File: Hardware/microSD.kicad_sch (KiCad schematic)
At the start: 6 parts, among them J3 Micro_SD_Card_Det, Q1 PMOS

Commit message: update
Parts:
- Q1: MPN (none) -> PNM723T201E0
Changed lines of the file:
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@@
+			)
+		)
+		(property "MPN" " PNM723T201E0"
+			(at 84.836 75.438 0)
+			(effects
+				(font
+					(size 1.27 1.27)
+				)
+				(hide yes)
 			)
 		)

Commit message: changes post 3rd review
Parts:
- Q1: footprint Package_TO_SOT_SMD:SOT-723 -> Package_TO_SOT_SMD:SOT-23; MPN PNM723T201E0 -> DMP3099L
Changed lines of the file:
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@@
 			)
 		)
-		(property "Footprint" "Package_TO_SOT_SMD:SOT-723"
+		(property "Footprint" "Package_TO_SOT_SMD:SOT-23"
 			(at 79.756 77.978 0)
 			(effects
@@
 			)
 		)
-		(property "MPN" " PNM723T201E0"
+		(property "MPN" " DMP3099L"
 			(at 84.836 75.438 0)
 			(effects

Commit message: post Andrei review, new SD
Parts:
- removed J3: Micro_SD_Card_Det, Connector_Card:microSD_HC_Hirose_DM3AT-SF-PEJM5, symbol Connector:Micro_SD_Card_Det
- added J9: ST1W008S4TR2000, iclr:JAE_ST1W008S4TR2000, symbol iclr:ST1W008S4TR2000
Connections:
- net SD1_DET is gone; now on net +3V3: R32.2
- net +3V3: no longer R32.1
- net GND: now also J9.GND1 (GND), J9.GND2 (GND), J9.GND3 (GND), J9.GND4 (GND)
- net SD1_CS: now also J9.C2
- net VSPI_MISO: now also J9.C7
- net VSPI_MOSI: now also J9.C3
- net VSPI_SCLK: now also J9.C5
- net at C49.1, JP2.2 (B), Q1.1 (D): now also J9.C4
- new net SD_DET: J9.C6, R32.1
- no-connect marks 2 -> 3
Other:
- moved on the sheet: C49, JP2, Q1, R33

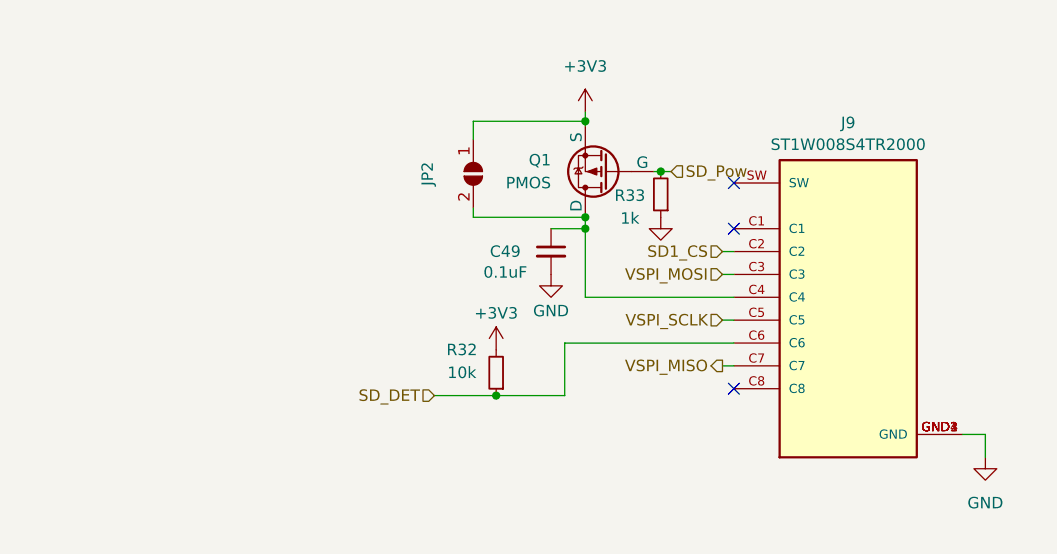
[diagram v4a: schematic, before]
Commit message: changed sd det pinout
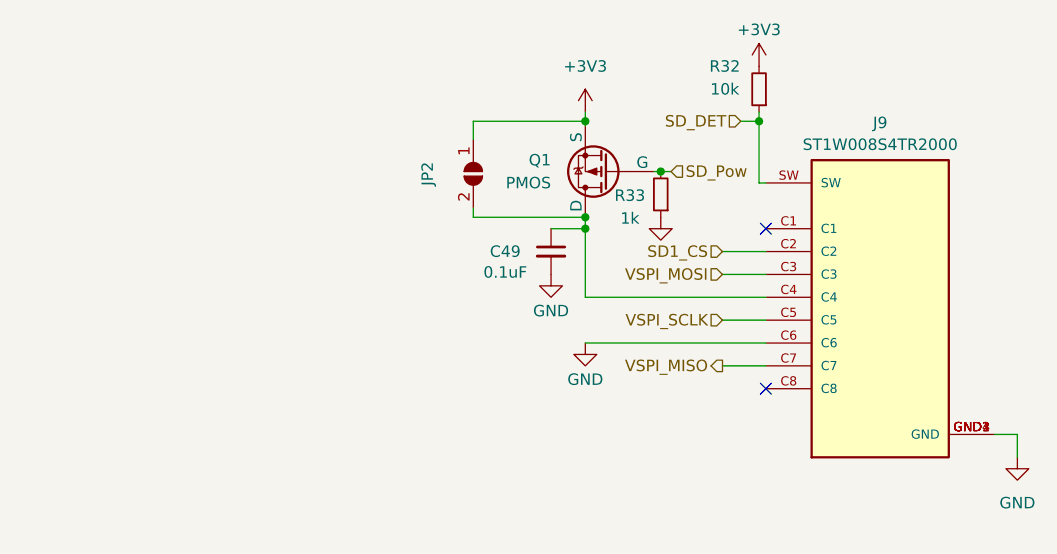
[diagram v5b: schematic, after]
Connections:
- net GND: now also J9.C6
- net SD_DET: now also J9.SW; no longer J9.C6
- no-connect marks 3 -> 2
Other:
- moved on the sheet: J9, R32

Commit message: updated jumpers and silkscreen labelling
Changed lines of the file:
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@@
 (kicad_sch
-	(version 20231120)
+	(version 20250114)
 	(generator "eeschema")
-	(generator_version "8.0")
+	(generator_version "9.0")
 	(paper "A4")
 	(junction
@@
 		(shape input)
 		(at 141.732 94.742 180)
-		(fields_autoplaced yes)
 		(effects
 			(font
@@
 		(shape output)
 		(at 141.732 99.822 180)
-		(fields_autoplaced yes)
 		(effects
 			(font
@@
 		(shape input)
 		(at 141.732 89.662 180)
-		(fields_autoplaced yes)
 		(effects
 			(font
@@
 		(shape input)
 		(at 141.732 87.122 180)
-		(fields_autoplaced yes)
 		(effects
 			(font
@@
 		(shape input)
 		(at 143.764 72.644 180)
-		(fields_autoplaced yes)
 		(effects
 			(font
@@
 		(shape input)
 		(at 136.017 78.232 0)
-		(fields_autoplaced yes)
-		(effects
-			(font
+		(effects
+			(font

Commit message: tidy up schematic and bom
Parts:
- C601: renamed from C49; value 0.1uF -> 100nF
- JP601: renamed from JP2; now left out of the parts list
- Q601: renamed from Q1; value PMOS -> DMP3099L
- R601: renamed from R33; value 1k -> 1kΩ
- R602: renamed from R32; value 10k -> 10kΩ
- renumbered J9 to J601
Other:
- moved on the sheet: JP601
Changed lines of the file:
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@@
 	(wire
 		(pts
-			(xy 114.046 74.676) (xy 114.046 72.644)
+			(xy 110.49 74.93) (xy 110.49 72.644)
 		)
 		(stroke
@@
 	(wire
 		(pts
-			(xy 114.046 83.312) (xy 114.046 82.296)
+			(xy 110.49 83.312) (xy 110.49 82.55)
 		)
 		(stroke
@@
 	(wire
 		(pts
-			(xy 114.046 72.644) (xy 126.492 72.644)
+			(xy 110.49 72.644) (xy 126.492 72.644)
 		)
 		(stroke
@@
 	(wire
 		(pts
-			(xy 126.492 83.312) (xy 114.046 83.312)
+			(xy 126.492 83.312) (xy 110.49 83.312)
 		)
 		(stroke
@@
 		(dnp no)
 		(fields_autoplaced yes)
-		(property "Reference" "#PWR082"
+		(property "Reference" "#PWR0602"
 			(at 126.492 75.438 0)
 			(effects
@@
 			(project "Ricardo-Kermit-Mini"
 				(path "/7db990e4-92e1-4f99-b4d2-435bbec1ba83/d2fb5c72-e348-4618-9c43-b5fd18c57de4"
-					(reference "#PWR082")
+					(reference "#PWR0602")
 					(unit 1)
 				)
@@
 		(on_board yes)
 		(dnp no)
-		(property "Reference" "R32"
+		(property "Reference" "R602"
 			(at 141.986 66.548 0)
 			(effects
@@
 			)
 		)
-		(property "Value" "10k"
+		(property "Value" "10kΩ"
 			(at 141.986 69.088 0)
 			(effects
@@
 			(project "Ricardo-Kermit-Mini"
 				(path "/7db990e4-92e1-4f99-b4d2-435bbec1ba83/d2fb5c72-e348-4618-9c43-b5fd18c57de4"
-					(reference "R32")
+					(reference "R602")
 					(unit 1)
 				)
@@
 	(symbol
 		(lib_id "Jumper:SolderJumper_2_Open")
-		(at 114.046 78.486 270)
+		(at 110.49 78.74 270)
 		(unit 1)
 		(exclude_from_sim no)
-		(in_bom yes)
+		(in_bom no)
 		(on_board yes)
 		(dnp no)
-		(property "Reference" "JP2"
-			(at 108.966 78.486 0)
+		(property "Reference" "JP601"
+			(at 105.41 78.74 0)
 			(effects
 				(font
@@
 		)
 		(property "Value" "SolderJumper_2_Open"
-			(at 82.296 60.706 0)
+			(at 78.74 60.96 0)
 			(effects
 				(font
@@
 		)
 		(property "Footprint" "iclr:SmallerSolderJP"
-			(at 114.046 78.486 0)
+			(at 110.49 78.74 0)
 			(effects
 				(font
@@
 		)
 		(property "Datasheet" "~"
-			(at 114.046 78.486 0)
+			(at 110.49 78.74 0)
 			(effects
 				(font
@@
 		)
 		(property "Description" ""
-			(at 114.046 78.486 0)
+			(at 110.49 78.74 0)
 			(effects
 				(font
@@
 			(project "Ricardo-Kermit-Mini"
 				(path "/7db990e4-92e1-4f99-b4d2-435bbec1ba83/d2fb5c72-e348-4618-9c43-b5fd18c57de4"
-					(reference "JP2")
+					(reference "JP601")
 					(unit 1)
 				)
@@
 		(dnp no)
 		(fields_autoplaced yes)
-		(property "Reference" "#PWR087"
+		(property "Reference" "#PWR0606"
 			(at 174.498 116.332 0)
 			(effects
@@
 			(project "Ricardo-Kermit-Mini"
 				(path "/7db990e4-92e1-4f99-b4d2-435bbec1ba83/d2fb5c72-e348-4618-9c43-b5fd18c57de4"
-					(reference "#PWR087")
+					(reference "#PWR0606")
 					(unit 1)
 				)
@@
 		(on_board yes)
 		(dnp no)
-		(property "Reference" "R33"
+		(property "Reference" "R601"
 			(at 131.445 80.9021 0)
 			(effects
@@
 			)
 		)
-		(property "Value" "1k"
+		(property "Value" "1kΩ"
 			(at 131.445 83.439 0)
 			(effects
@@
 			(project "Ricardo-Kermit-Mini"
 				(path "/7db990e4-92e1-4f99-b4d2-435bbec1ba83/d2fb5c72-e348-4618-9c43-b5fd18c57de4"
-					(reference "R33")
+					(reference "R601")
 					(unit 1)
 				)
@@
 		(dnp no)
 		(fields_autoplaced yes)
-		(property "Reference" "#PWR085"
+		(property "Reference" "#PWR0604"
 			(at 134.874 89.662 0)
 			(effects
@@
 			(project "Ricardo-Kermit-Mini"
 				(path "/7db990e4-92e1-4f99-b4d2-435bbec1ba83/d2fb5c72-e348-4618-9c43-b5fd18c57de4"
-					(reference "#PWR085")
+					(reference "#PWR0604")
 					(unit 1)
 				)
@@
 		(dnp no)
 		(fields_autoplaced yes)
-		(property "Reference" "Q1"
-			(at 122.682 76.962 0)
+		(property "Reference" "Q601"
+			(at 123.19 76.9619 0)
 			(effects
 				(font
@@
 			)
 		)
-		(property "Value" "PMOS"
-			(at 122.682 79.502 0)
+		(property "Value" "DMP3099L"
+			(at 123.19 79.5019 0)
 			(effects
 				(font
@@
 			(project "Ricardo-Kermit-Mini"
 				(path "/7db990e4-92e1-4f99-b4d2-435bbec1ba83/d2fb5c72-e348-4618-9c43-b5fd18c57de4"
-					(reference "Q1")
+					(reference "Q601")
 					(unit 1)
 				)
@@
 		(dnp no)
 		(fields_autoplaced yes)
-		(property "Reference" "J9"
+		(property "Reference" "J601"
 			(at 159.258 72.8175 0)
 			(effects
@@
 			(project "Ricardo-Kermit-Mini"
 				(path "/7db990e4-92e1-4f99-b4d2-435bbec1ba83/d2fb5c72-e348-4618-9c43-b5fd18c57de4"
-					(reference "J9")
+					(reference "J601")
 					(unit 1)
 				)
@@
 		(on_board yes)
 		(dnp no)
-		(property "Reference" "#PWR084"
+		(property "Reference" "#PWR0603"
 			(at 126.492 103.632 0)
 			(effects
@@
 			(project "Ricardo-Kermit-Mini"
 				(path "/7db990e4-92e1-4f99-b4d2-435bbec1ba83/d2fb5c72-e348-4618-9c43-b5fd18c57de4"
-					(reference "#PWR084")
+					(reference "#PWR0603")
 					(unit 1)
 				)
@@
 		(on_board yes)
 		(dnp no)
-		(property "Reference" "C49"
+		(property "Reference" "C601"
 			(at 117.602 87.122 0)
 			(effects
@@
 			)
 		)
-		(property "Value" "0.1uF"
+		(property "Value" "100nF"
 			(at 117.602 89.4334 0)
 			(effects
@@
 			(project "Ricardo-Kermit-Mini"
 				(path "/7db990e4-92e1-4f99-b4d2-435bbec1ba83/d2fb5c72-e348-4618-9c43-b5fd18c57de4"
-					(reference "C49")
+					(reference "C601")
 					(unit 1)
 				)
@@
 		(on_board yes)
 		(dnp no)
-		(property "Reference" "#PWR083"
+		(property "Reference" "#PWR0605"
 			(at 145.796 70.358 0)
 			(effects
@@
 			(project "Ricardo-Kermit-Mini"
 				(path "/7db990e4-92e1-4f99-b4d2-435bbec1ba83/d2fb5c72-e348-4618-9c43-b5fd18c57de4"
-					(reference "#PWR083")
+					(reference "#PWR0605")
 					(unit 1)
 				)
@@
 		(on_board yes)
 		(dnp no)
-		(property "Reference" "#PWR081"
+		(property "Reference" "#PWR0601"
 			(at 122.682 96.012 0)
 			(effects
@@
 			(project "Ricardo-Kermit-Mini"
 				(path "/7db990e4-92e1-4f99-b4d2-435bbec1ba83/d2fb5c72-e348-4618-9c43-b5fd18c57de4"
-					(reference "#PWR081")
+					(reference "#PWR0601")
 					(unit 1)
 				)
